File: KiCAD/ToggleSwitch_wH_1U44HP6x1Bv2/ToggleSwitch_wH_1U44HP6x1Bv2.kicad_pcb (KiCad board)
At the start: 2 copper layers, 223.2 x 39.7 mm, 29 parts, among them SW1 SW_M6/M6.35_Panel_Mount_Hole, SW2 SW_M6/M6.35_Panel_Mount_Hole, SW3 SW_M6/M6.35_Panel_Mount_Hole, SW4 SW_M6/M6.35_Panel_Mount_Hole, SW5 SW_M6/M6.35_Panel_Mount_Hole, SW6 SW_M6/M6.35_Panel_Mount_Hole

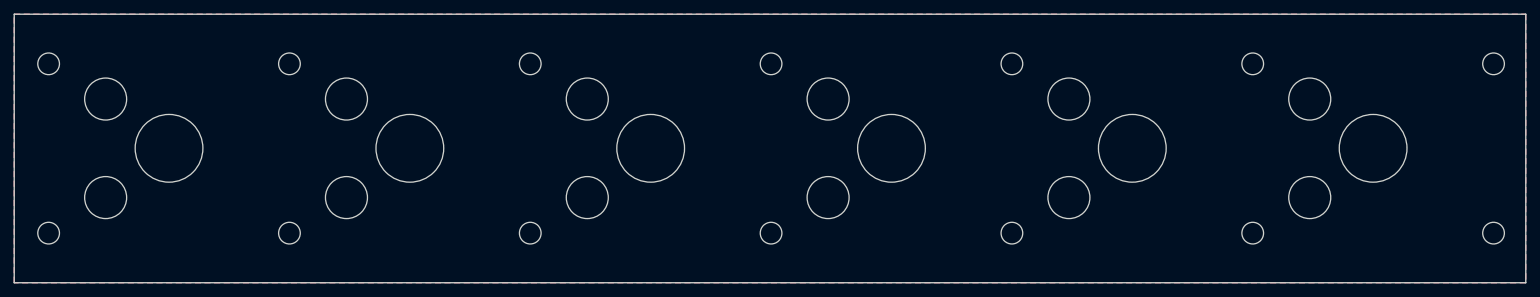
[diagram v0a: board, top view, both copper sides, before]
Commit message: updated all modules to use plated through-holes wherever possible
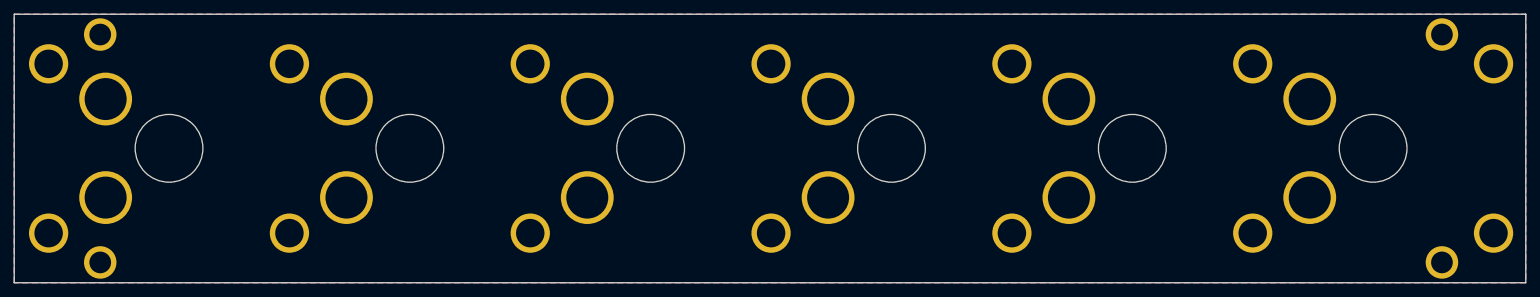
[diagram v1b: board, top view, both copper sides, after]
